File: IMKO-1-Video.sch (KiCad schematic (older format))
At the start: 29 parts, among them J9 CONN_VIDEO, U18 82S129, U19 74LS244, U20 74LS244, U22 74LS32, U23 74LS86, U24 74LS163, U25 74LS00, U26 74LS374, U8 SFF96364, X2 1MHz

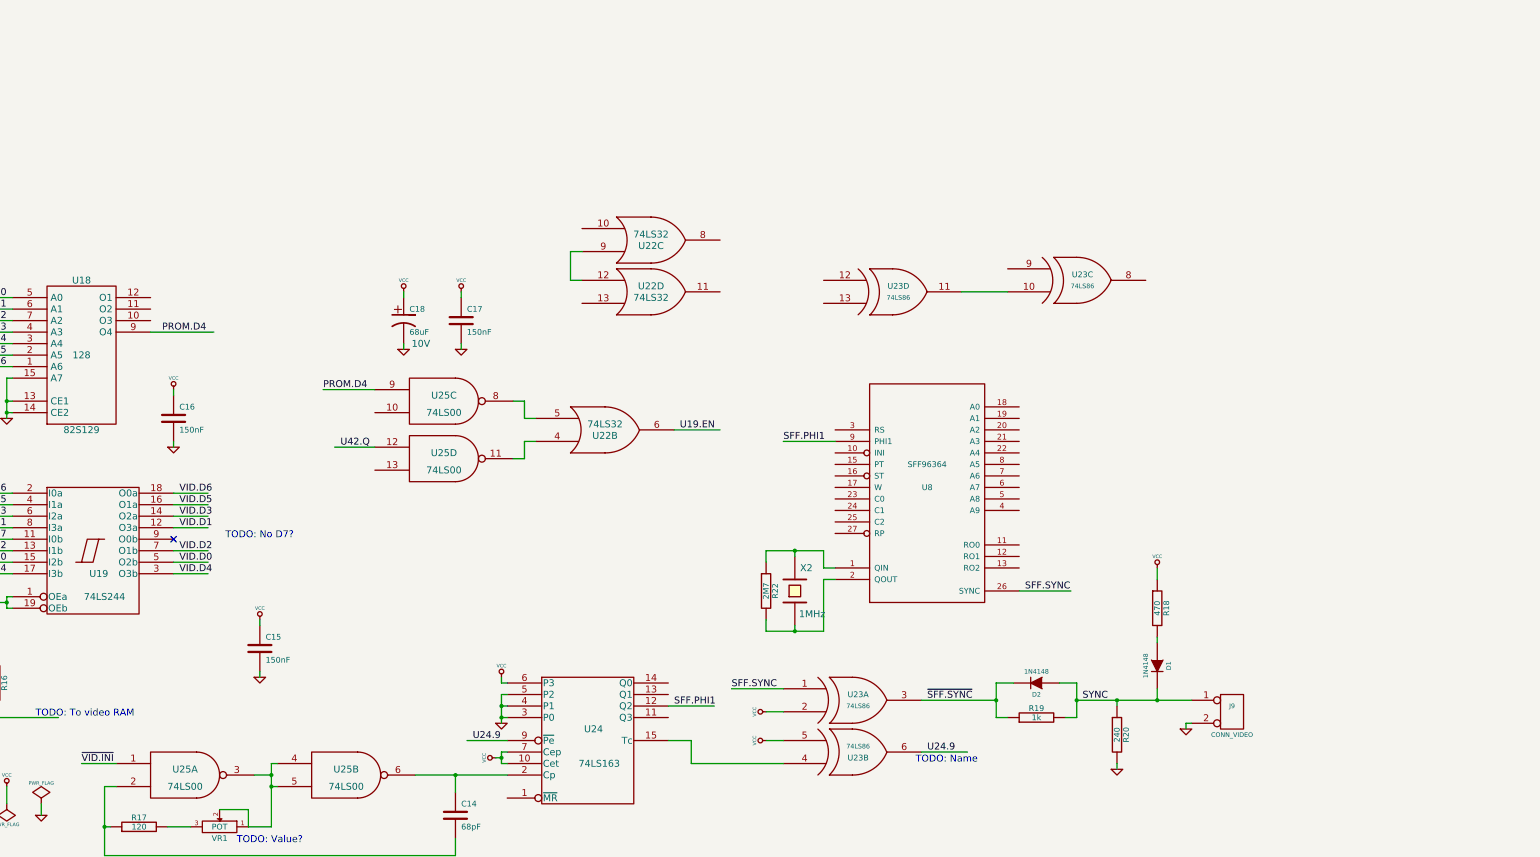
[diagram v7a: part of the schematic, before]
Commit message: Added U21
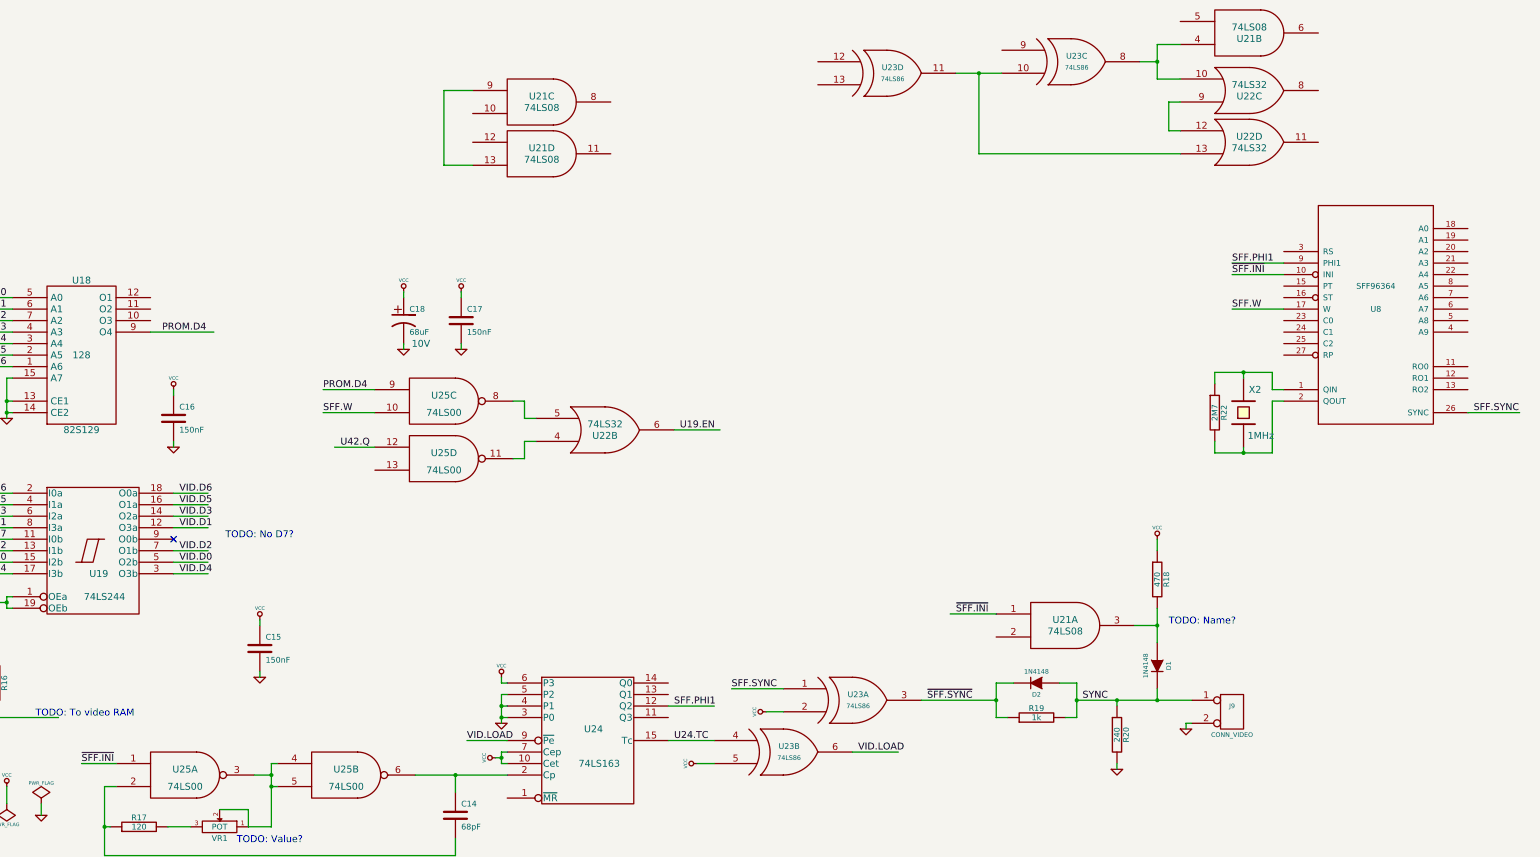
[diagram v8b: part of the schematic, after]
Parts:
- added U21: 74LS08, symbol 74LS08
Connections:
- net labels added: SFF.W, U24.TC, VID.LOAD, ~SFF.INI
- net labels removed: U24.9, ~VID.INI
- wire segments 180 -> 192
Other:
- note added: "TODO: Name?"
- note removed: "TODO: Name"
- moved on the sheet: R18, R22, U22C, U22D, U23B, U23C, U23D, U8, X2
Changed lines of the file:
@@
-EESchema Schematic File Version 2  date Fri 12 Oct 2012 08:34:01 PM EEST
+EESchema Schematic File Version 2  date Fri 12 Oct 2012 09:40:08 PM EEST
 LIBS:power
 LIBS:device
@@
 L 74LS86 U23
 U 2 1 5075BC07
-P 11350 7500
-F 0 "U23" H 11400 7550 50  0000 C CNN
-F 1 "74LS86" H 11400 7450 40  0000 C CNN
-	2    11350 7500
-	1    0    0    1
+P 10750 7500
+F 0 "U23" H 10800 7550 50  0000 C CNN
+F 1 "74LS86" H 10800 7450 40  0000 C CNN
+	2    10750 7500
+	1    0    0    -1
 $EndComp
 $Comp
 L 74LS86 U23
 U 3 1 5075BC19
-P 13300 3400
-F 0 "U23" H 13350 3450 50  0000 C CNN
-F 1 "74LS86" H 13350 3350 40  0000 C CNN
-	3    13300 3400
+P 13250 1500
+F 0 "U23" H 13300 1550 50  0000 C CNN
+F 1 "74LS86" H 13300 1450 40  0000 C CNN
+	3    13250 1500
 	1    0    0    -1
 $EndComp
@@
 L 74LS86 U23
 U 4 1 5075BC2B
-P 11700 3500
-F 0 "U23" H 11750 3550 50  0000 C CNN
-F 1 "74LS86" H 11750 3450 40  0000 C CNN
-	4    11700 3500
+P 11650 1600
+F 0 "U23" H 11700 1650 50  0000 C CNN
+F 1 "74LS86" H 11700 1550 40  0000 C CNN
+	4    11650 1600
 	1    0    0    -1
 $EndComp
@@
 	10750 7150 10600 7150
 Wire Wire Line
-	10750 7400 10600 7400
-Wire Wire Line
-	9750 7400 9950 7400
-Wire Wire Line
-	9950 7400 9950 7600
-Wire Wire Line
-	9950 7600 10750 7600
-Wire Wire Line
-	11950 7500 12350 7500
-Text Label 12000 7500 0    60   ~ 0
-U24.9
+	10150 7600 10000 7600
+Wire Wire Line
+	9750 7400 10150 7400
+Wire Wire Line
+	11350 7500 11750 7500
 Wire Wire Line
 	8350 7400 8000 7400
-Text Label 8050 7400 0    60   ~ 0
-U24.9
-Text Notes 11900 7600 0    60   ~ 0
-TODO: Name
 $Comp
 L 74LS32 U22
@@
 L 74LS32 U22
 U 3 1 5075CDB4
-P 9600 3050
-F 0 "U22" H 9600 3100 60  0000 C CNN
-F 1 "74LS32" H 9600 3000 60  0000 C CNN
-	3    9600 3050
+P 14800 1750
+F 0 "U22" H 14800 1800 60  0000 C CNN
+F 1 "74LS32" H 14800 1700 60  0000 C CNN
+	3    14800 1750
 	1    0    0    1
 $EndComp
@@
 L 74LS32 U22
 U 4 1 5075CDCD
-P 9600 3500
-F 0 "U22" H 9600 3550 60  0000 C CNN
-F 1 "74LS32" H 9600 3450 60  0000 C CNN
-	4    9600 3500
+P 14800 2200
+F 0 "U22" H 14800 2250 60  0000 C CNN
+F 1 "74LS32" H 14800 2150 60  0000 C CNN
+	4    14800 2200
 	1    0    0    -1
 $EndComp
@@
 Wire Wire Line
 	4650 7600 4950 7600
-Text Label 4650 7600 0    60   ~ 0
-~VID.INI
 $Comp
 L SFF96364 U8
 U 1 1 50771E3D
-P 12000 5100
-F 0 "U8" H 12000 5000 50  0000 C CNN
-F 1 "SFF96364" H 12000 5200 50  0000 C CNN
-F 2 "MODULE" H 12000 5100 50  0001 C CNN
-F 3 "DOCUMENTATION" H 12000 5100 50  0001 C CNN
-	1    12000 5100
+P 15900 3550
+F 0 "U8" H 15900 3450 50  0000 C CNN
+F 1 "SFF96364" H 15900 3650 50  0000 C CNN
+F 2 "MODULE" H 15900 3550 50  0001 C CNN
+F 3 "DOCUMENTATION" H 15900 3550 50  0001 C CNN
+	1    15900 3550
 	1    0    0    -1
 $EndComp
@@
 L CRYSTAL X2
 U 1 1 50771E58
-P 10850 6100
-F 0 "X2" V 11050 6000 60  0000 C CNN
-F 1 "1MHz" V 10650 5950 60  0000 C CNN
-	1    10850 6100
+P 14750 4550
+F 0 "X2" V 14950 4450 60  0000 C CNN
+F 1 "1MHz" V 14550 4400 60  0000 C CNN
+	1    14750 4550
 	0    -1   -1   0
 $EndComp
@@
 L R R22
 U 1 1 50771E7D
-P 10600 6100
-F 0 "R22" V 10680 6100 50  0000 C CNN
-F 1 "2M7" V 10600 6100 50  0000 C CNN
-	1    10600 6100
-	1    0    0    -1
-$EndComp
-Wire Wire Line
-	10600 6350 10600 6450
-Wire Wire Line
-	10600 5850 10600 5750
-Wire Wire Line
-	10600 5750 11100 5750
-Wire Wire Line
-	10850 5750 10850 5800
-Wire Wire Line
-	10600 6450 11100 6450
-Wire Wire Line
-	10850 6450 10850 6400
-Wire Wire Line
-	11100 5750 11100 5900
-Wire Wire Line
-	11100 5900 11200 5900
-Connection ~ 10850 5750
-Wire Wire Line
-	11100 6450 11100 6000
-Wire Wire Line
-	11100 6000 11200 6000
-Connection ~ 10850 6450
-Wire Wire Line
-	11200 4800 10750 4800
-Text Label 10750 4800 0    60   ~ 0
+P 14500 4550
+F 0 "R22" V 14580 4550 50  0000 C CNN
+F 1 "2M7" V 14500 4550 50  0000 C CNN
+	1    14500 4550
+	1    0    0    -1
+$EndComp
+Wire Wire Line
+	14500 4800 14500 4900
+Wire Wire Line
+	14500 4300 14500 4200
+Wire Wire Line
+	14500 4200 15000 4200
+Wire Wire Line
+	14750 4200 14750 4250
+Wire Wire Line
+	14500 4900 15000 4900
+Wire Wire Line
+	14750 4900 14750 4850
+Wire Wire Line
+	15000 4200 15000 4350
+Wire Wire Line
+	15000 4350 15100 4350
+Connection ~ 14750 4200
+Wire Wire Line
+	15000 4900 15000 4450
+Wire Wire Line
+	15000 4450 15100 4450
+Connection ~ 14750 4900
+Wire Wire Line
+	15100 3250 14650 3250
+Text Label 14650 3250 0    60   ~ 0
 SFF.PHI1
 Text Label 9800 7100 0    60   ~ 0
@@
 	9750 7100 10150 7100
 Wire Wire Line
-	9000 3150 8900 3150
-Wire Wire Line
-	8900 3150 8900 3400
-Wire Wire Line
-	8900 3400 9000 3400
-Wire Wire Line
-	12800 6100 13250 6100
-Text Label 12850 6100 0    60   ~ 0
+	14200 1850 14100 1850
+Wire Wire Line
+	14100 1850 14100 2100
+Wire Wire Line
+	14100 2100 14200 2100
+Wire Wire Line
+	16700 4550 17150 4550
+Text Label 16750 4550 0    60   ~ 0
 SFF.SYNC
 Text Label 10300 6950 0    60   ~ 0
@@
 	10300 6950 10750 6950
 Wire Wire Line
-	12300 3500 12700 3500
+	12250 1600 12650 1600
 $Comp
 L VCC #PWR023
@@
 L VCC #PWR024
 U 1 1 50784997
-P 10600 7400
-F 0 "#PWR024" H 10600 7500 30  0001 C CNN
-F 1 "VCC" H 10600 7500 30  0000 C CNN
-	1    10600 7400
-	0    -1   -1   0
+P 10000 7600
+F 0 "#PWR024" H 10000 7700 30  0001 C CNN
+F 1 "VCC" H 10000 7700 30  0000 C CNN
+	1    10000 7600
+	0    -1   1    0
 $EndComp
 Wire Wire Line
@@
 L R R18
 U 1 1 507858D1
-P 14000 6250
-F 0 "R18" V 14080 6250 50  0000 C CNN
-F 1 "470" V 14000 6250 50  0000 C CNN
-	1    14000 6250
+P 14000 6000
+F 0 "R18" V 14080 6000 50  0000 C CNN
+F 1 "470" V 14000 6000 50  0000 C CNN
+	1    14000 6000
 	1    0    0    -1
 $EndComp
@@
 L VCC #PWR026
 U 1 1 507858D7
-P 14000 5900
-F 0 "#PWR026" H 14000 6000 30  0001 C CNN
-F 1 "VCC" H 14000 6000 30  0000 C CNN
-	1    14000 5900
-	1    0    0    -1
-$EndComp
-Wire Wire Line
-	14000 5900 14000 6000
-Wire Wire Line
-	14000 6500 14000 6550
+P 14000 5650
+F 0 "#PWR026" H 14000 5750 30  0001 C CNN
+F 1 "VCC" H 14000 5750 30  0000 C CNN
+	1    14000 5650
+	1    0    0    -1
+$EndComp
+Wire Wire Line
+	14000 5650 14000 5750
+Wire Wire Line
+	14000 6250 14000 6550
 $Comp
 L GND #PWR027
@@
 Wire Wire Line
 	14250 7250 14250 7300
+Wire Wire Line
+	15100 3350 14650 3350
+Text Label 14650 3350 0    60   ~ 0
+~SFF.INI
+Text Label 4650 7600 0    60   ~ 0
+~SFF.INI
+$Comp
+L 74LS08 U21
+U 1 1 507860F7
+P 13200 6400
+F 0 "U21" H 13200 6450 60  0000 C CNN
+F 1 "74LS08" H 13200 6350 60  0000 C CNN
+	1    13200 6400
+	1    0    0    -1
+$EndComp
+$Comp
+L 74LS08 U21
+U 2 1 50786110
+P 14800 1250
+F 0 "U21" H 14800 1300 60  0000 C CNN
+F 1 "74LS08" H 14800 1200 60  0000 C CNN
+	2    14800 1250
+	1    0    0    1
+$EndComp
+$Comp
+L 74LS08 U21
+U 3 1 50786122
+P 8650 1850
+F 0 "U21" H 8650 1900 60  0000 C CNN
+F 1 "74LS08" H 8650 1800 60  0000 C CNN
+	3    8650 1850
+	1    0    0    -1
+$EndComp
+$Comp
+L 74LS08 U21
+U 4 1 50786134
+P 8650 2300
+F 0 "U21" H 8650 2350 60  0000 C CNN
+F 1 "74LS08" H 8650 2250 60  0000 C CNN
+	4    8650 2300
+	1    0    0    -1
+$EndComp
+Text Label 12250 6300 0    60   ~ 0
+~SFF.INI
+Wire Wire Line
+	12600 6300 12200 6300
+Wire Wire Line
+	13800 6400 14000 6400
+Connection ~ 14000 6400
+Text Notes 14100 6400 0    60   ~ 0
+TODO: Name?
+Wire Wire Line
+	15100 3650 14650 3650
+Text Label 14650 3650 0    60   ~ 0
+SFF.W
+Text Label 6750 4550 0    60   ~ 0
+SFF.W
+Wire Wire Line
+	6750 4550 7200 4550
+Text Label 9800 7400 0    60   ~ 0
+U24.TC
+Text Label 11400 7500 0    60   ~ 0
+VID.LOAD
+Text Label 8000 7400 0    60   ~ 0
+VID.LOAD
+Wire Wire Line
+	7800 1750 7800 2400
+Wire Wire Line
+	7800 2400 8050 2400
+Wire Wire Line
+	7800 1750 8050 1750
+Wire Wire Line
+	14200 1350 14000 1350
+Wire Wire Line
+	14000 1350 14000 1650
+Wire Wire Line
+	14000 1500 13850 1500
+Wire Wire Line
+	14000 1650 14200 1650
+Connection ~ 14000 1500
+Wire Wire Line
+	12450 1600 12450 2300
+Wire Wire Line
+	12450 2300 14200 2300
+Connection ~ 12450 1600
 $EndSCHEMATC
